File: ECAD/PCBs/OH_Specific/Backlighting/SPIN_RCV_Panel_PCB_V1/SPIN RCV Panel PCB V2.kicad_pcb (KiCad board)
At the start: 2 copper layers, 45.7 x 168.3 mm, 66 parts, among them J1 Conn_01x04_Female, J2 Conn_01x04_Female

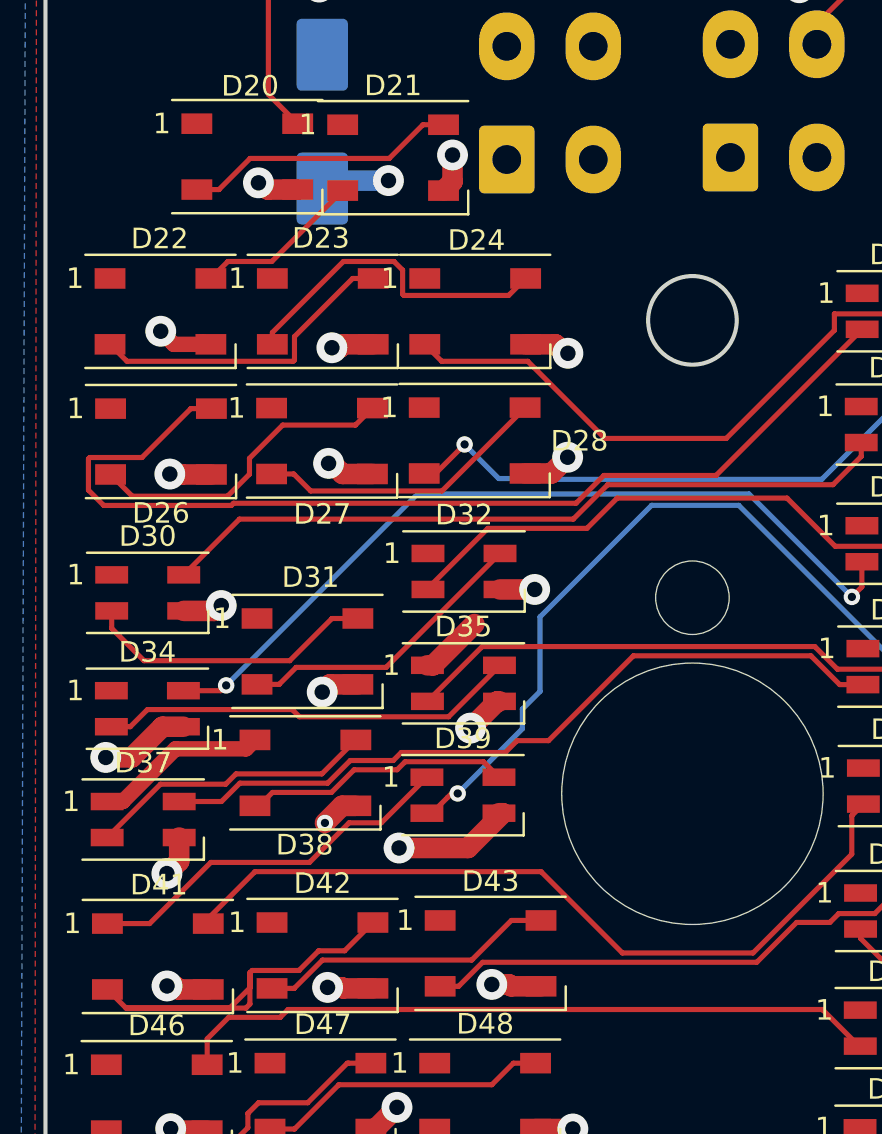
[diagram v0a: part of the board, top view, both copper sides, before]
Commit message: SPIN RCV Panel Backlighting
Changed - Silkscreen to V2.1
Changed - Manufacturing files organised and updated to match V2.1 board design.
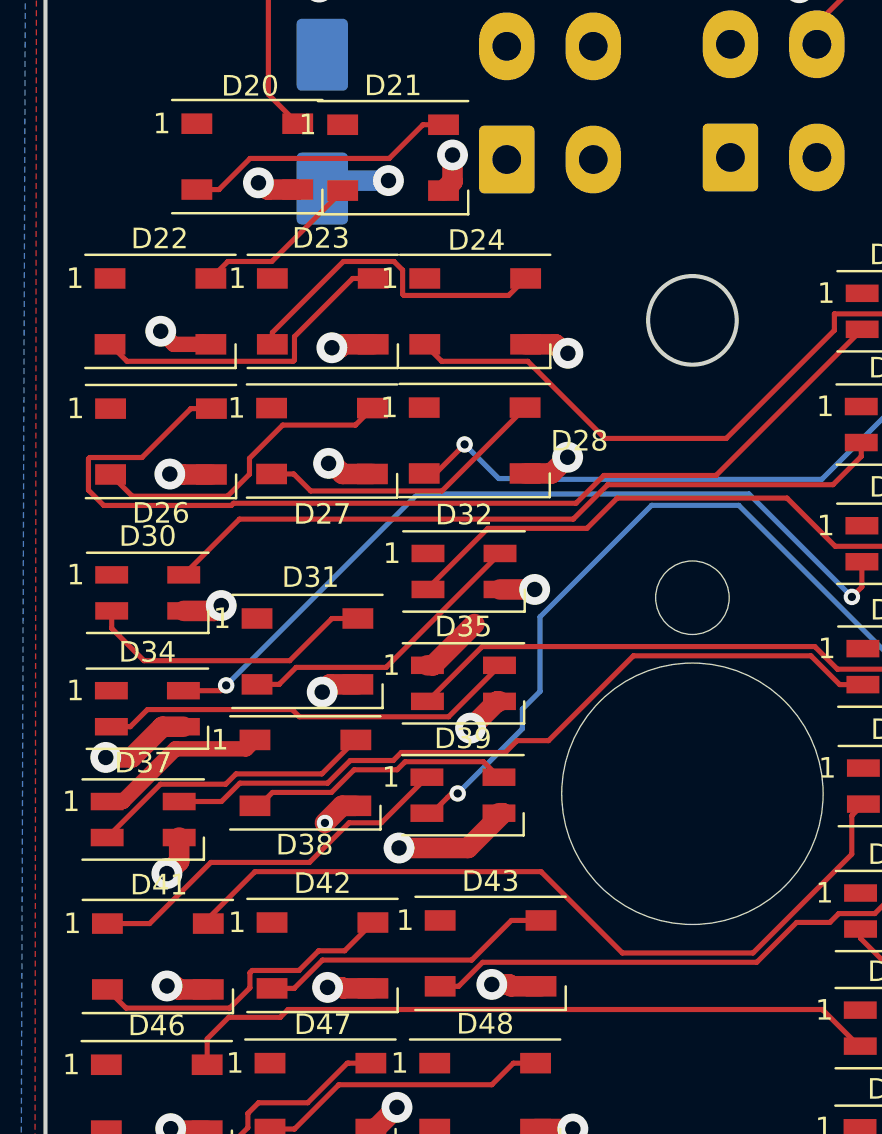
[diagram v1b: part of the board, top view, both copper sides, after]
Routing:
- net Net-(D41-Pad2): track 23.0 -> 15.4 mm
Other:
- board text added: "Version 2.1"
- board text removed: "Version 2.0"
